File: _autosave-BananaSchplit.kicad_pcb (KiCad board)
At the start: 2 copper layers, 59.1 x 73 mm, 71 parts, among them J1 Screw_Terminal_01x02, J2 Screw_Terminal_01x02, J3 Screw_Terminal_01x02, J4 Screw_Terminal_01x02, J5 Conn_02x08_Odd_Even, J6 Conn_02x08_Odd_Even, J7 Conn_02x08_Odd_Even, J8 Barrel_Jack, P1 USB_C_Plug_USB2.0, Q1 AO3407A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

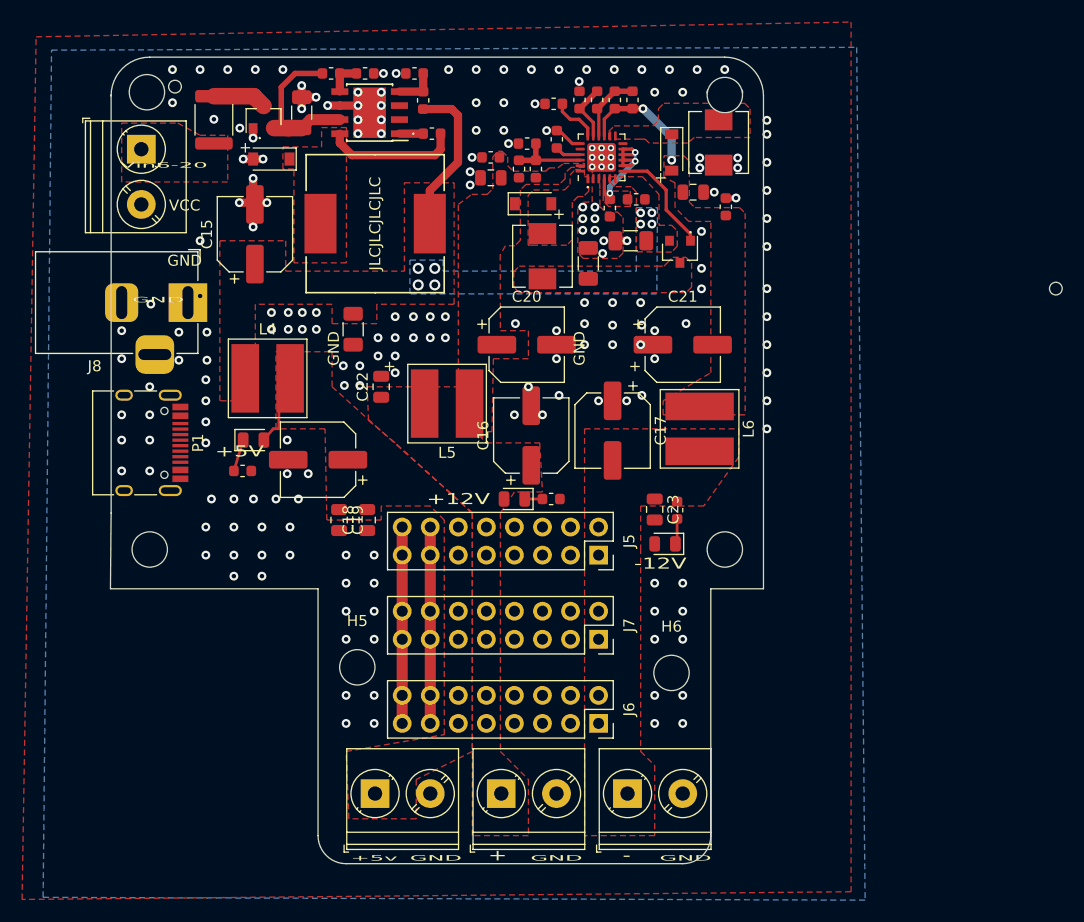
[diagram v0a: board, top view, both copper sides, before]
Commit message: filtering + euroheaders
added more filtering/capacitance.
changed layout, added eurroack power headers and more inputs
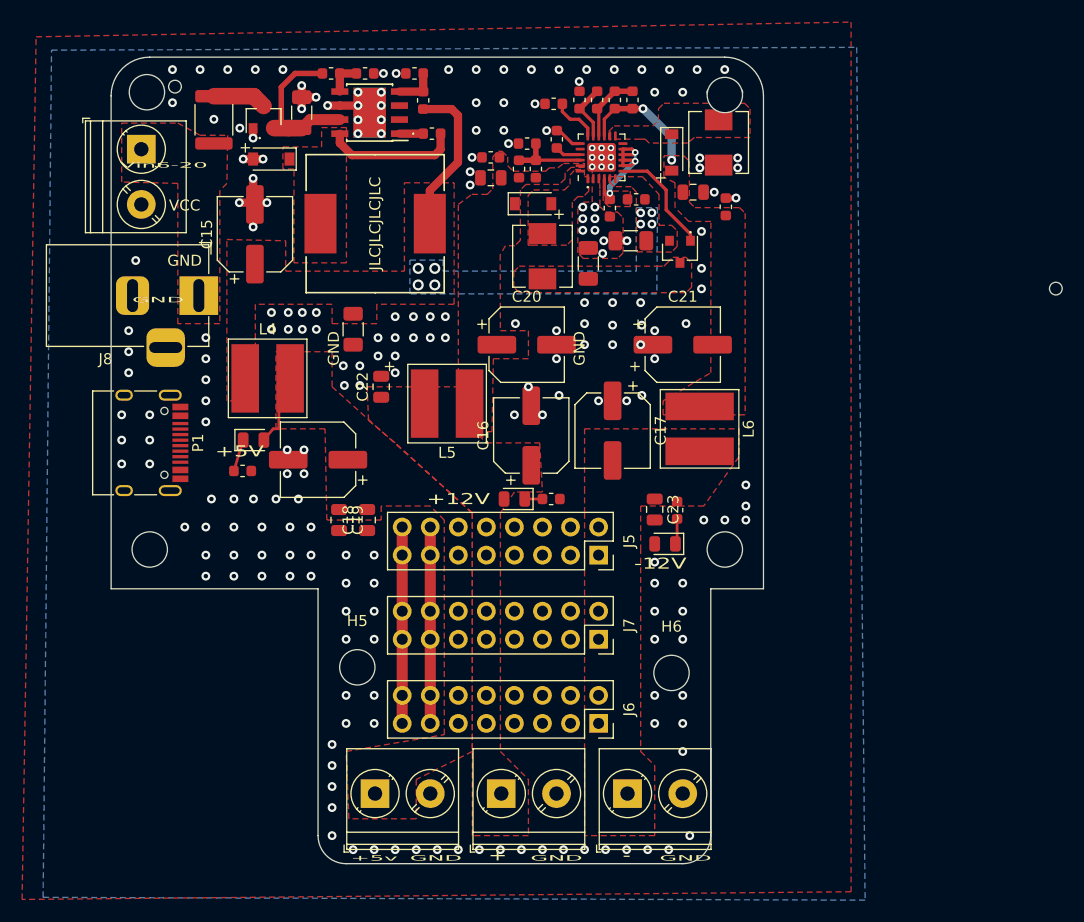
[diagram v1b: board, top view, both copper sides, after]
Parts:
- moved J8 1.17 mm to (32.4, 37.5)
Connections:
- J8 pad 1: Net-(J8-Pad1) -> VCC
- J8 pad 2: Net-(J8-Pad2) -> GND
- P1 pad B5: Net-(P1-PadB5) -> powertosplit
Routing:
- net VCC: vias 0 -> 1
- net Net-(J8-Pad2): vias 1 -> 0
- net Net-(J8-Pad1): vias 1 -> 0
- net GND: vias 184 -> 217
- net (no net): vias 14 -> 2
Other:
- outline, holes or cut-outs redrawn
- board text removed: "450mA MAX"
